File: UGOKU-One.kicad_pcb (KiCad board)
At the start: 2 copper layers, 70 x 70 mm, 84 parts, among them J1 Conn_01x04, J10 Conn_01x02, J11 USB_C_Receptacle_USB2.0_16P, J12 Conn_01x02, J13 Conn_01x02, J2 SERVO, J3 Conn_02x03_Odd_Even, J4 Conn_01x10, J5 SERVO, J6 Conn_01x02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

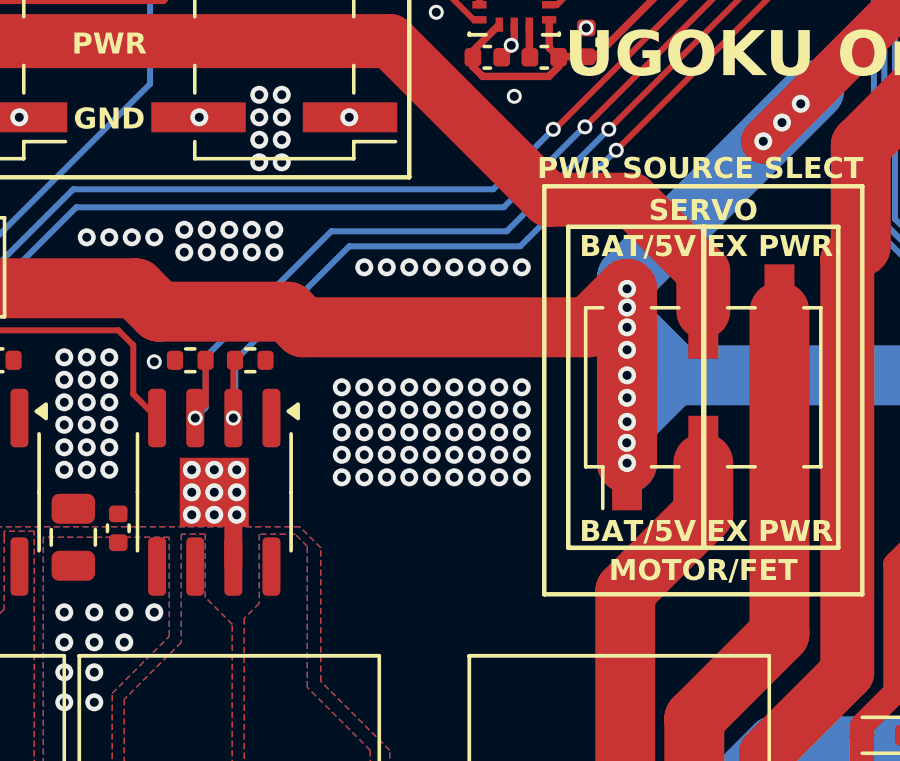
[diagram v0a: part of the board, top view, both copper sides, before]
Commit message: 5V電源でアクチュエータを駆動する際の安定性および安全性向上のためにのためにTVSダイオードと電解コンデンサを追加 PCB上に配置（未配線）
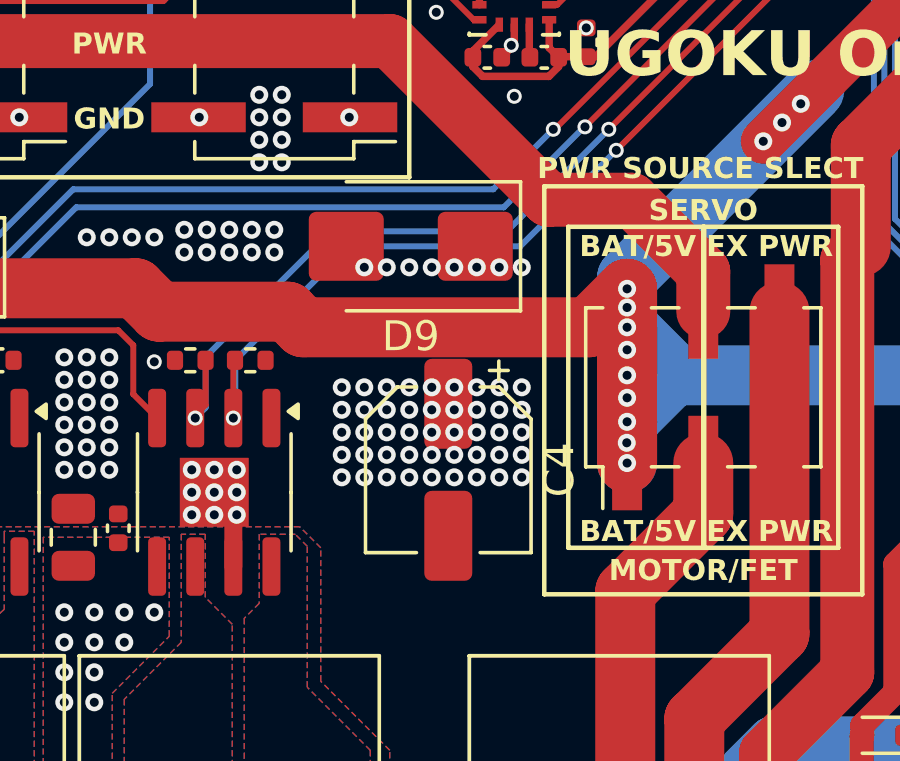
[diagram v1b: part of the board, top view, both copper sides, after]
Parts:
- added C4: C_Polarized, Capacitor_SMD:CP_Elec_5x5.4, F.Cu at (-2.20, 15.8)
- added D9: SMBJ5.5A, Diode_SMD:D_SMB, F.Cu at (-3.45, 8.30)
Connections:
- net BAT_5V renamed Net-(BT1-+)
- net PWR renamed EX_PWR

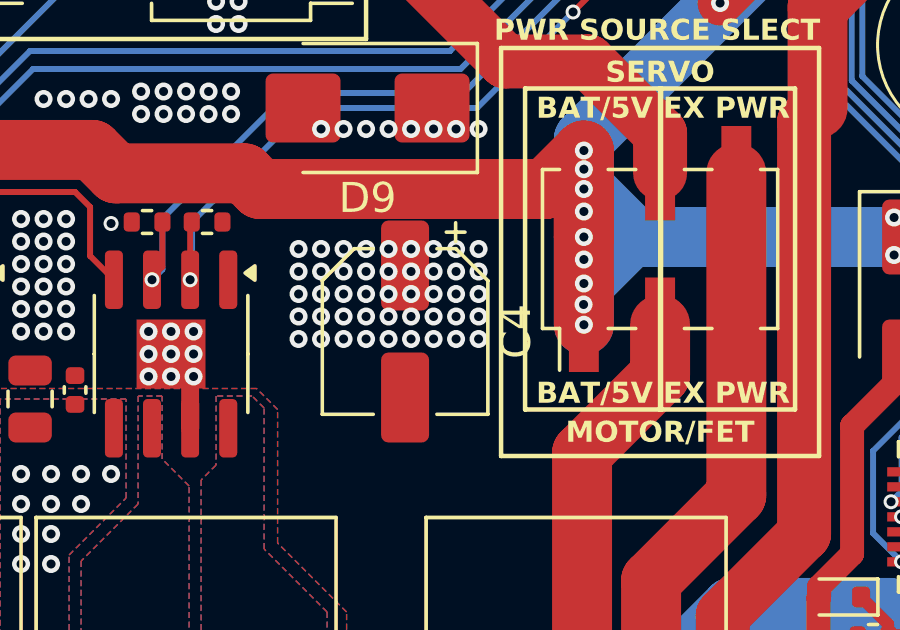
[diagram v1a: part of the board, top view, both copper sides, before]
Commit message: TVSダイオードをSMBJ6.0に変更
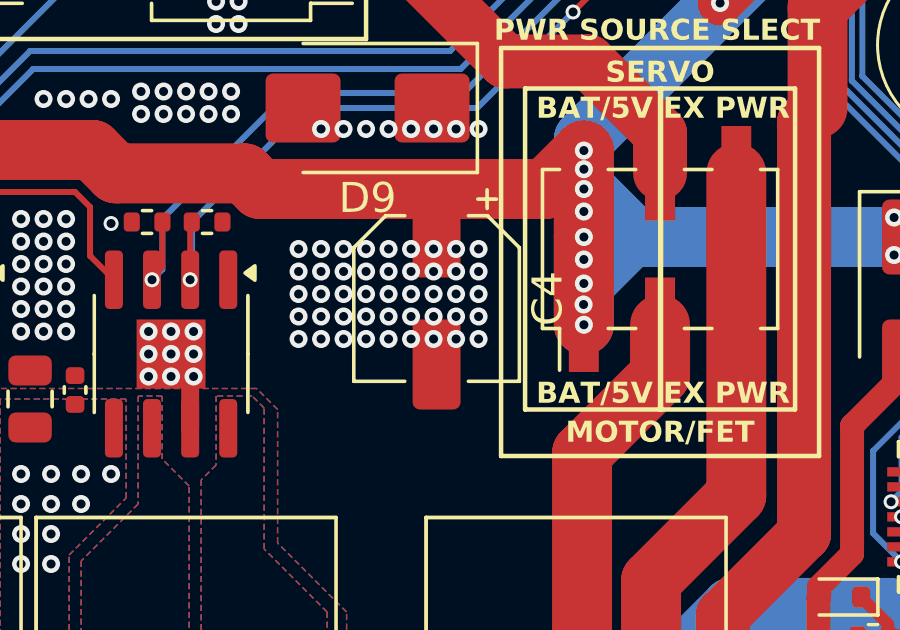
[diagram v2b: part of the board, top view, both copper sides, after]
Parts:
- moved C4 1.52 mm to (-1.15, 14.7)
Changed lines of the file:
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@@
 			)
 		)
+		(property "LCSC" "C113976"
+			(at 0 0 0)
+			(layer "F.SilkS")
+			(hide yes)
+			(effects
+				(font
+					(size 1.27 1.27)
+					(thickness 0.15)
+				)
+			)
+		)
 		(property ki_fp_filters "TO-???* *_Diode_* *SingleDiode* D_*")
 		(sheetname "/")
@@
 	(footprint "Capacitor_SMD:CP_Elec_5x5.4"
 		(layer "F.Cu")
-		(at -2.2 15.75 -90)
+		(at -1.15 14.65 -90)
 		(descr "SMD capacitor, aluminum electrolytic, Nichicon, 5.0x5.4mm")
 		(tags "capacitor electrolytic")
@@
 			(hide yes)
 			(effects
+				(font
+					(size 1.27 1.27)
+					(thickness 0.15)
+				)
+			)
+		)
+		(property "LCSC" "C18221498"
+			(at 0 0 0)
+			(layer "F.SilkS")
+			(hide yes)
+			(effects

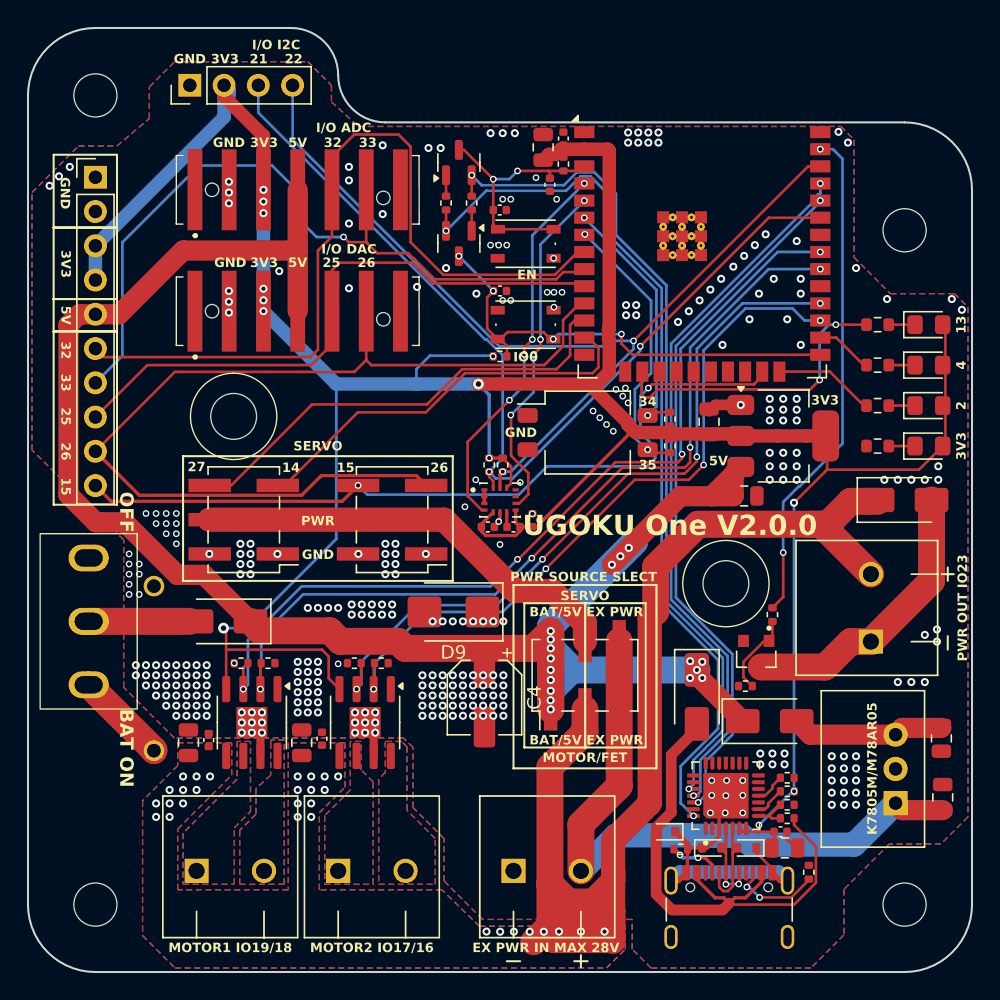
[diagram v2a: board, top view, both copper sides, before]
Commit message: 5VラインのコンデンサとTVSダイオードの配線を実施 IMUをBMI270に戻し
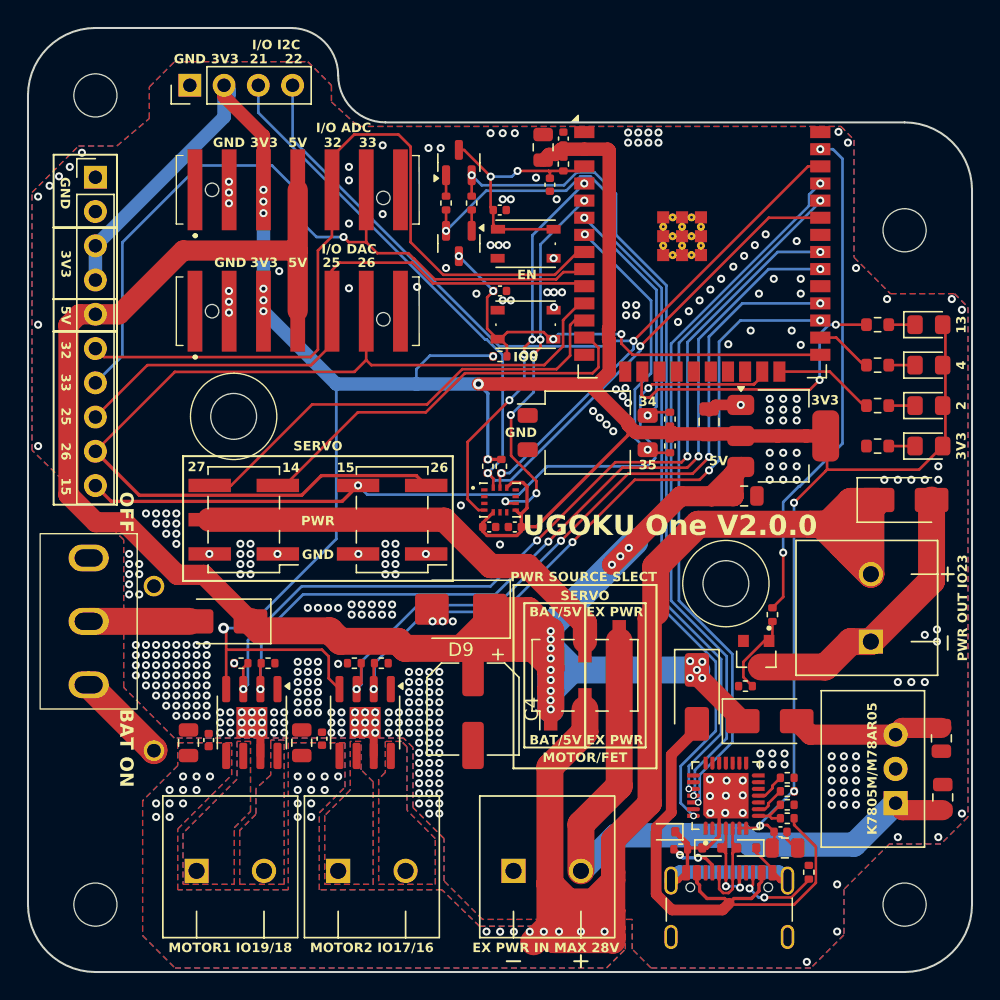
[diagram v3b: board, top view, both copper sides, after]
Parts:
- removed C13: 10nF, Capacitor_SMD:C_0402_1005Metric
- removed C14: 0.1uF, Capacitor_SMD:C_0402_1005Metric
- removed C15: 2.2uF, Capacitor_SMD:C_0402_1005Metric
- removed MT1: ICM-42605, 0_UGOKU-One_Lib:XDCR_ICM-42605
- removed R27, R28: 10k, Resistor_SMD:R_0402_1005Metric
- added C20: 0.1uF, Capacitor_SMD:C_0402_1005Metric, F.Cu at (-0.80, 2.00)
- added C21: 0.1uF, Capacitor_SMD:C_0402_1005Metric, F.Cu at (1.10, 2.00)
- added R2: 10k, Resistor_SMD:R_0402_1005Metric, F.Cu at (0.10, -2.50)
- added R3: 10k, Resistor_SMD:R_0402_1005Metric, F.Cu at (-0.90, -2.50)
- added U7: BMI270, 0_UGOKU-One_Lib:XDCR_BMI270, F.Cu at (0.00, 0.00)
- C4: value C_Polarized -> 470μF; footprint Capacitor_SMD:CP_Elec_5x5.4 -> Capacitor_SMD:CP_Elec_6.3x7.7
- D9: value SMBJ5.5A -> SMBJ6.5A
- moved C4 1.20 mm to (-2.00, 15.5)
- moved D9 0.59 mm to (-2.90, 8.10)
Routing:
- net 5V: track 140.9 -> 158.7 mm
- net MOT_PWR: track 92.7 -> 106.8 mm
- net GND: track 35.5 -> 32.2 mm, vias 330 -> 377
- net INT2: track 25.8 -> 28.1 mm, vias 4 -> 6
- net 3V3: track 232.9 -> 233.8 mm
- net USB_5V: track 39.8 -> 40.5 mm
- net MD2_IN2: track 53.2 -> 52.6 mm
- net Net-(D4-A2): track 7.08 -> 7.62 mm

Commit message: 配線、ビア、シルクスクリーンの修正
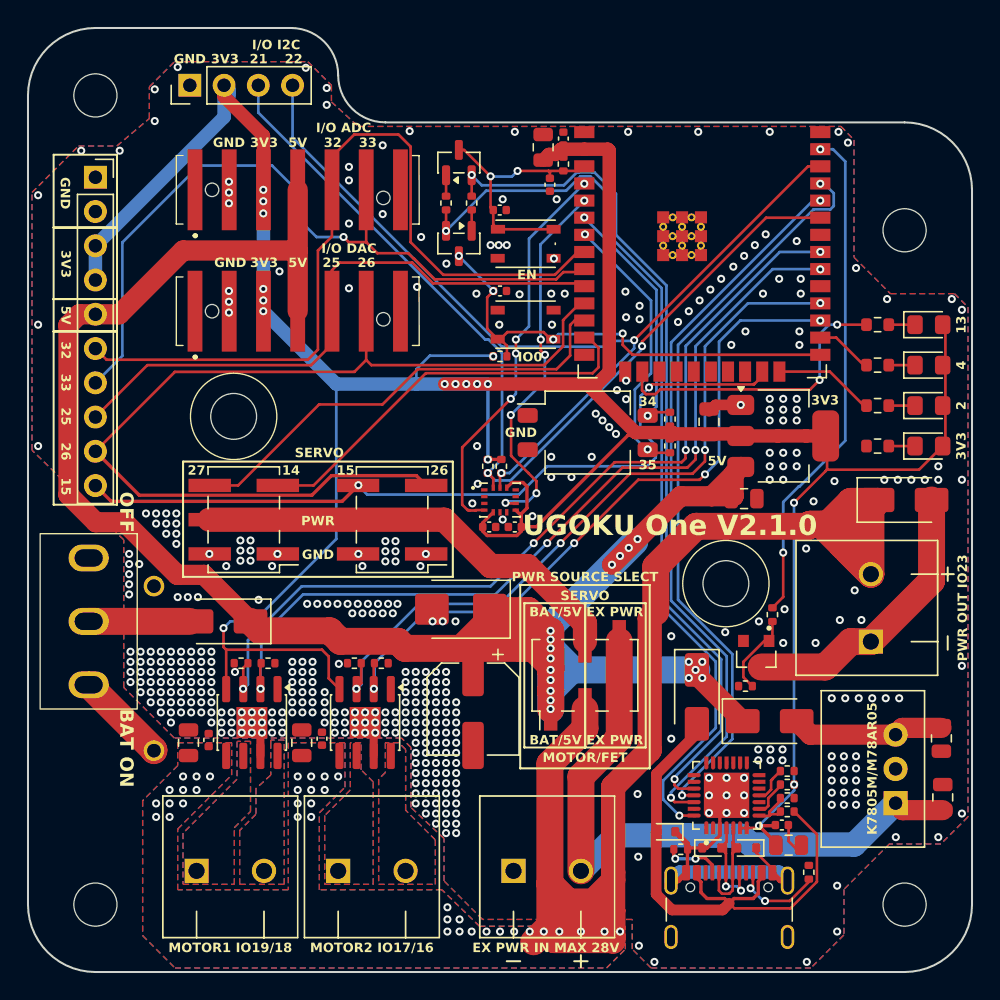
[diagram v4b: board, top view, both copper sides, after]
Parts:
- J4: footprint Connector_PinHeader_2.54mm:PinHeader_1x10_P2.54mm_Vertical -> Connector_PinSocket_2.54mm:PinSocket_1x10_P2.54mm_Vertical
- moved C3 0.51 mm to (20.9, 24.1)
- moved R13 0.50 mm to (21.3, 21.1)
- moved R14 0.50 mm to (21.3, 23.1)
- moved R15 0.50 mm to (21.3, 22.1)
- moved R16 0.50 mm to (21.3, 20.1)
- moved C2 0.34 mm to (21.4, 25.6)
- moved C1 0.20 mm to (18.1, -0.10)
- moved U2 0.06 mm to (16.8, 21.9)
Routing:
- net 3V3: track 233.8 -> 236.7 mm, vias 13 -> 17
- net RXD: track 52.7 -> 55.6 mm
- net RXD0: track 51.7 -> 54.5 mm
- net Net-(Q2-E): track 62.0 -> 63.7 mm
- net Net-(Q3-E): track 66.7 -> 68.4 mm
- net USB_5V: track 40.5 -> 41.4 mm
- net INT1: track 28.6 -> 29.4 mm
- net Net-(U2-VBUS): track 2.88 -> 3.44 mm
- net Net-(U2-~{SUSPEND}): track 2.30 -> 2.80 mm
- net GND: track 32.2 -> 32.6 mm, vias 377 -> 439
- net MOT_PWR: vias 30 -> 37
- net 5V: vias 17 -> 18
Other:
- board text added: "UGOKU One V2.1.0"
- board text added: "UGOKU One Ver 2.1.0 UGOKU Lab 2025-12"
- board text removed: "UGOKU One V2.0.0"
- board text removed: "UGOKU One Ver 2.0.0 UGOKU Lab 2025-8"

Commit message: ベタGNDとviaを修正
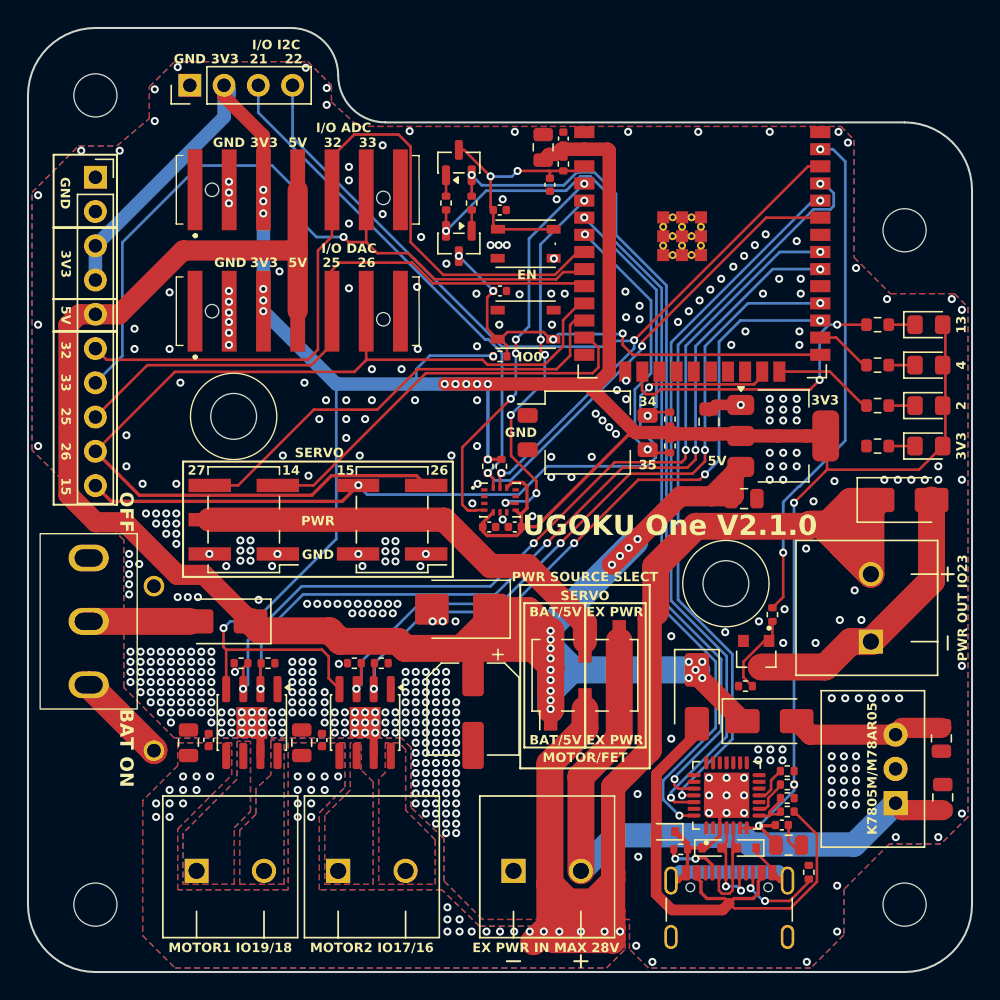
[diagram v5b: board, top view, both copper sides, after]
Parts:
- moved C17 0.10 mm to (-13.2, 17.8)
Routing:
- net GND: vias 439 -> 469

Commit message: ベタGNDを修正
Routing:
- net GND: vias 469 -> 470
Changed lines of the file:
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@@
 	)
 	(via
+		(at -16.3 -11.1)
+		(size 0.6)
+		(drill 0.3)
+		(layers "F.Cu" "B.Cu")
+		(free yes)
+		(net 2)
+	)
+	(via
 		(at -14.5 -8.7)
 		(size 0.6)
@@
 	)
 	(via
-		(at -0.1 -18.9)
+		(at 1.4 -17.6)
 		(size 0.6)
 		(drill 0.3)
@@
 	)
 	(via
-		(at -11.2 -15.7)
-		(size 0.6)
-		(drill 0.3)
-		(layers "F.Cu" "B.Cu")
-		(free yes)
-		(net 2)
-	)
-	(via
 		(at 8.675 -8.15)
 		(size 0.6)
@@
 	)
 	(via
-		(at 0.5 -18.9)
+		(at 1.4 -19.3)
 		(size 0.6)
 		(drill 0.3)
@@
 	)
 	(via
-		(at -0.7 -18.9)
+		(at -2.1 -18.7)
 		(size 0.6)
 		(drill 0.3)
@@
 	)
 	(via
+		(at -14.6 -27.4)
+		(size 0.6)
+		(drill 0.3)
+		(layers "F.Cu" "B.Cu")
+		(free yes)
+		(net 2)
+	)
+	(via
 		(at 23.4 10.6)
 		(size 0.6)
@@
 	)
 	(segment
-		(start 15.2 -2.87)
-		(end 14.28 -1.95)
+		(start -10.635 14.025)
+		(end -10.635 12.445)
 		(width 0.2)
 		(layer "F.Cu")
@@
 	)
 	(segment
-		(start 9.6375 -1.95)
-		(end 4.5 3.1875)
+		(start 15.2 -2.87)
+		(end 14.28 -1.95)
 		(width 0.2)
 		(layer "F.Cu")
@@
 	)
 	(segment
-		(start -10.635 13.935)
-		(end -10.29 13.59)
+		(start 9.6375 -1.95)
+		(end 4.5 3.1875)
 		(width 0.2)
 		(layer "F.Cu")
@@
 	)
 	(segment
-		(start -10.29 13.59)
-		(end -10.29 12.1)
-		(width 0.2)
-		(layer "F.Cu")
-		(net 38)
-	)
-	(segment
 		(start 4.5 3.1875)
 		(end 4.5 3.2)
@@
 	)
 	(segment
-		(start -10.635 14.025)
-		(end -10.635 13.935)
+		(start -10.635 12.445)
+		(end -10.29 12.1)
 		(width 0.2)
 		(layer "F.Cu")
@@
 	)
 	(segment
-		(start 15.2 -11.4)
-		(end 18.38 -14.58)
+		(start -6 7.7)
+		(end -10.6 12.3)
 		(width 0.2)
 		(layer "B.Cu")
@@
 	)
 	(segment
-		(start -10.29 13.68)
-		(end -10.635 14.025)
+		(start 15.2 -11.4)
+		(end 18.38 -14.58)
 		(width 0.2)
 		(layer "B.Cu")
@@
 	)
 	(segment
-		(start -6 7.7)
-		(end -10.29 11.99)
+		(start -10.6 12.3)
+		(end -10.6 13.99)
 		(width 0.2)
 		(layer "B.Cu")
@@
 	)
 	(segment
-		(start 4.5 3.2)
-		(end 0 7.7)
+		(start 0 7.7)
+		(end -6 7.7)
 		(width 0.2)
 		(layer "B.Cu")
@@
 	)
 	(segment
-		(start -10.29 11.99)
-		(end -10.29 13.68)
+		(start 4.5 3.2)
+		(end 0 7.7)
 		(width 0.2)
 		(layer "B.Cu")
@@
 	)
 	(segment
-		(start 0 7.7)
-		(end -6 7.7)
+		(start -10.6 13.99)
+		(end -10.635 14.025)
 		(width 0.2)
 		(layer "B.Cu")
